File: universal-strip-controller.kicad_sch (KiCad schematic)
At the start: 50 parts, among them J1 Conn_01x03_Pin, J2 Conn_01x02_Pin, SW1 434133025816, SW2 434133025816, U1 RP2350B, U2 RPI RM2, U3 W25Q128JVSIQ, U9 DS3231SN, X1 12MHz

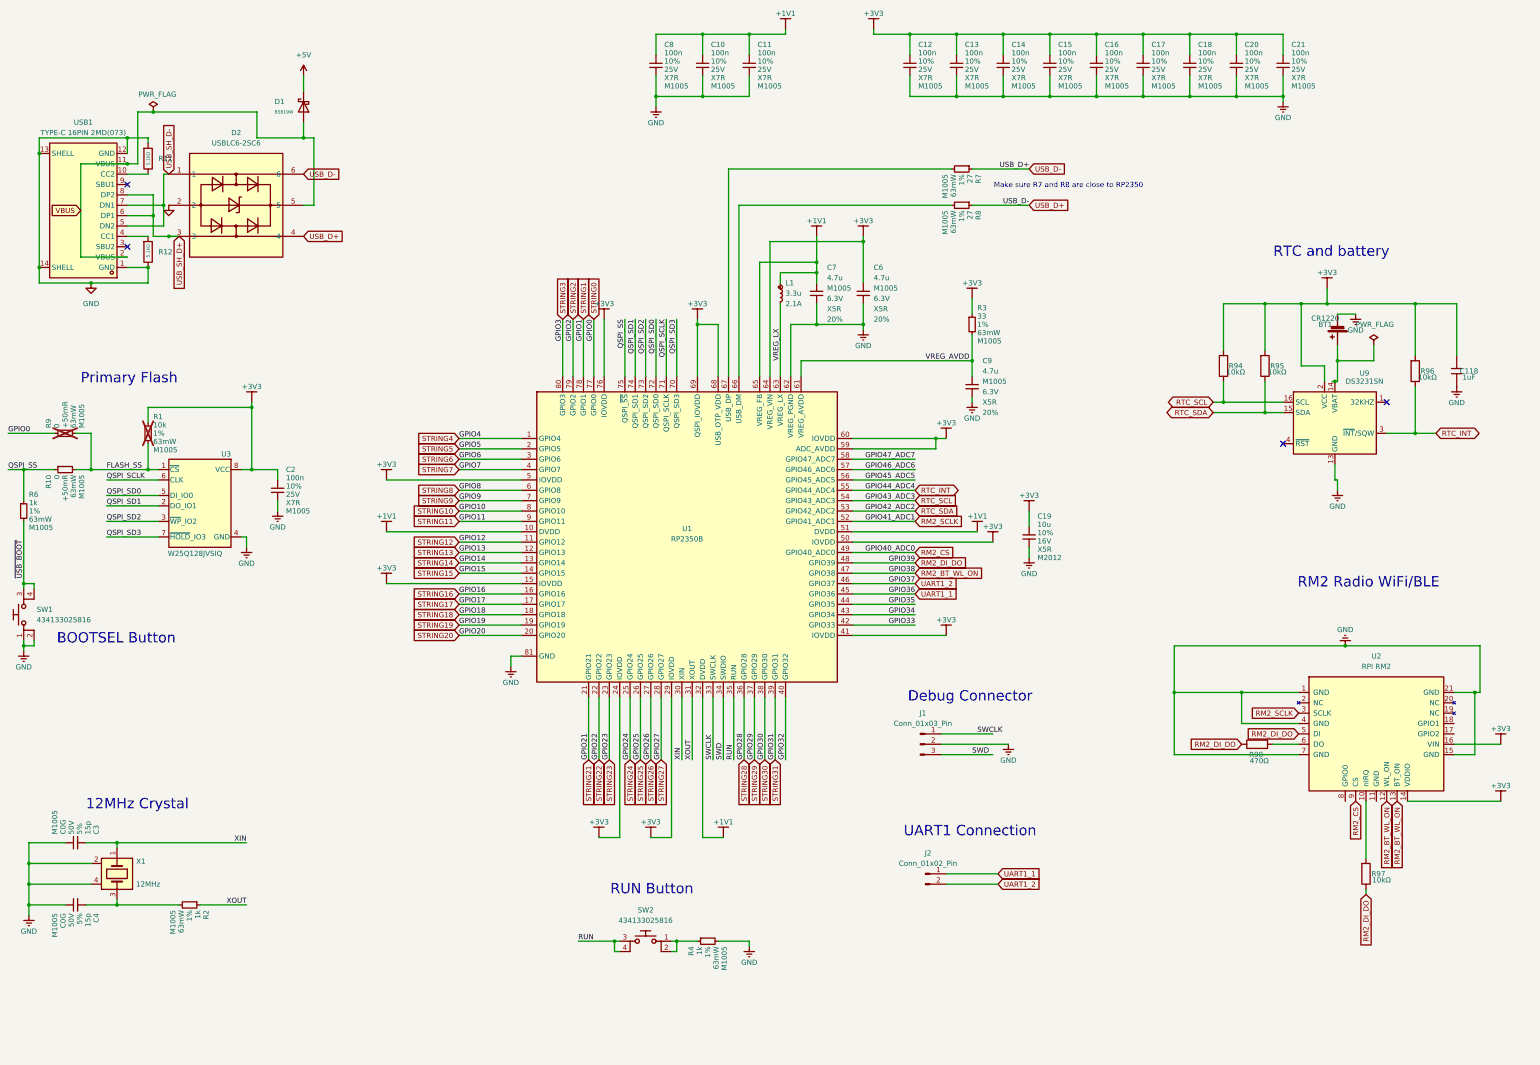
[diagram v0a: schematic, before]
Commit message: Added power, output, and more status LEDs
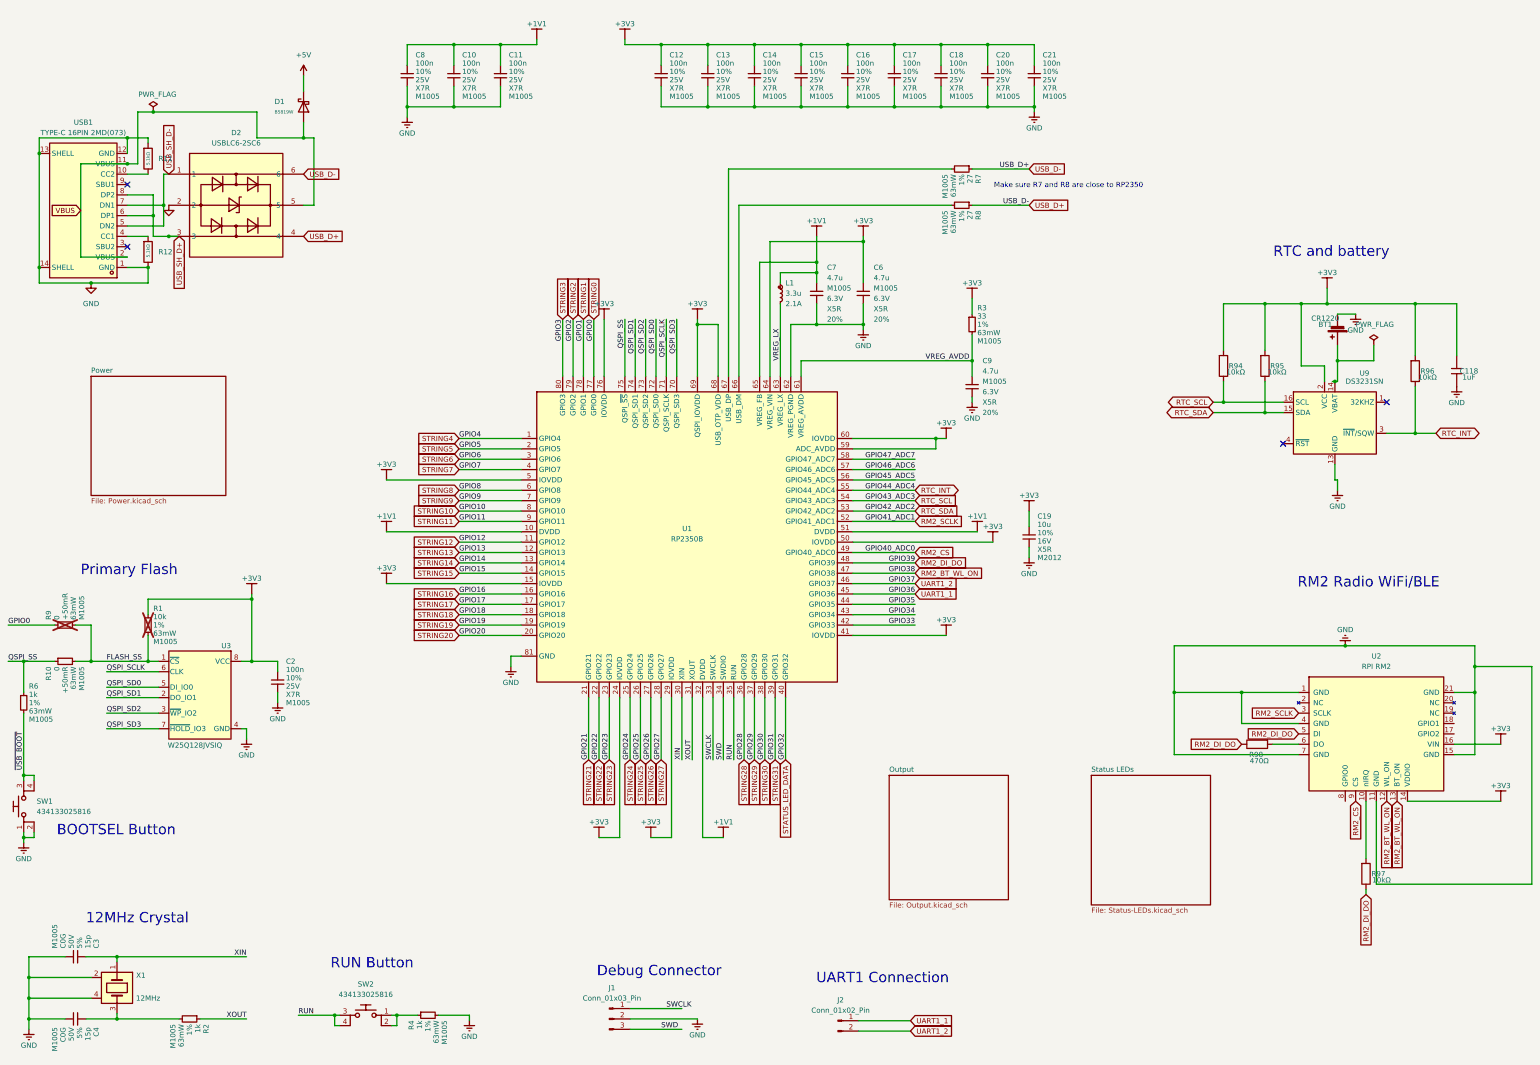
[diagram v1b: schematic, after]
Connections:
- net GND: now also U2.11 (GND)
- net GPIO32 renamed STATUS_LED_DATA
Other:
- added sheet Output (Output.kicad_sch)
- added sheet Power (Power.kicad_sch)
- added sheet Status LEDs (Status-LEDs.kicad_sch)
- moved on the sheet: C10, C11, C12, C13, C14, C15, C16, C17, C18, C2, C20, C21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

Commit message: Fix ERC: register missing libraries, add PWR_FLAGs, rename zone rails
- Register project-local sym-lib-table/fp-lib-table. PixelBlit points at
  pico-pixel's live library; RPI_COMPILED/KiCad_Standard/EasyEDA/PCM_JLCPCB
  footprints vendored (via the abandoned universal-strip-controller-first
  attempt) into libs/; RPI_DB, RPI - Power, EasyEDA, PCM_JLCPCB-Diodes and
  PCM_JLCPCB-Resistors symbols extracted from the schematics' own embedded
  symbol cache into standalone .kicad_sym files, validated with
  `kicad-cli sym upgrade`.
- Fix U1's footprint: RPI_COMPILED:rpi_rp2350b doesn't exist anywhere
  (not even in the original RP2350B-MINIMAL reference) - corrected to
  rpi_rp2350b_vias, the footprint that's actually there.
- Point D10 (BZT52C15V) and R5/R20 (0603s) at KiCad's own standard
  SOD-123/0603 footprints; no vendored copy of their original
  EasyEDA/JLCPCB footprints existed anywhere to source from.
- Add PWR_FLAGs on the 8 nets ERC found undriven: +VIN_Z1-4, +12V_SYS,
  GND (top sheet), +1V1, and VREG_AVDD (U1 pin 61).
- Rename +12V_Z1-4 to +VIN_Z1-4 (zones carry 5-12V depending on what's
  plugged in, not a fixed 12V).

ERC: 1009 violations / 8 errors -> 533 violations / 0 errors.
Remaining warnings are pre-existing: fuse/diode symbols typed
Unspecified instead of Passive (pin_to_pin), intentional dual net
labels (STRINGn/GPIOn etc., except a real USB_D+/USB_D- issue still
open), schematic drawing hygiene (off-grid/dangling wire endpoints),
and symbol-cache drift now visible now that real libraries exist
(lib_symbol_mismatch - fix via Update Symbols from Library in KiCad).
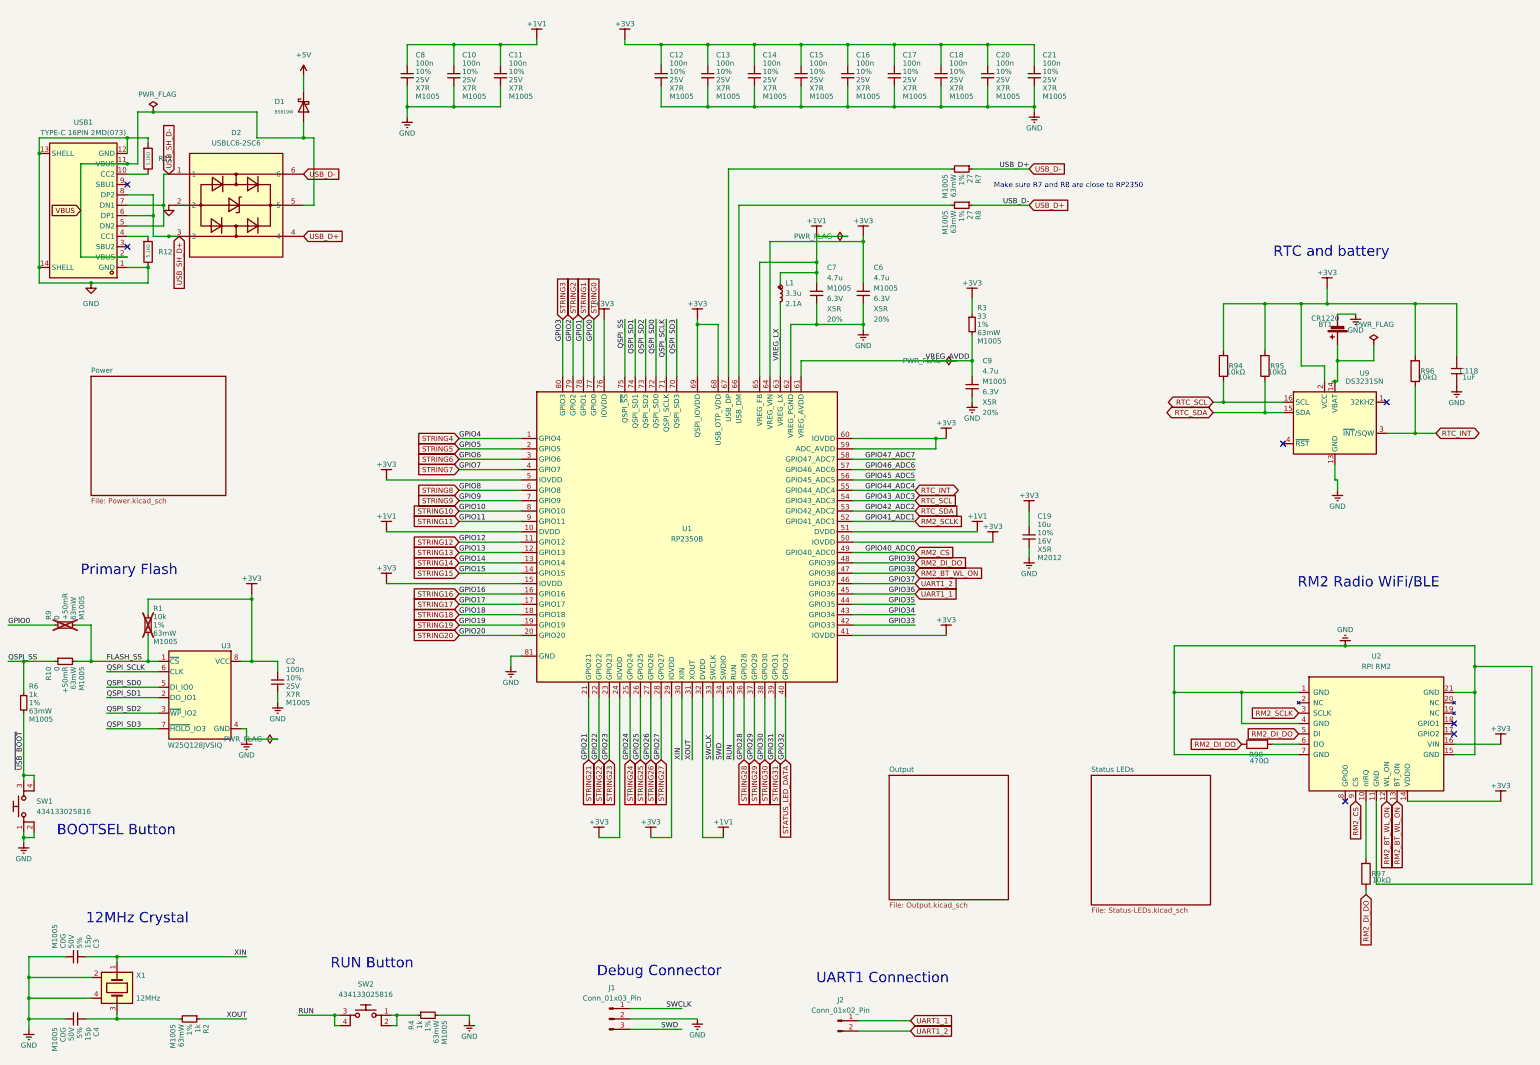
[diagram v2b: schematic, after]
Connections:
- no-connect marks 4 -> 7

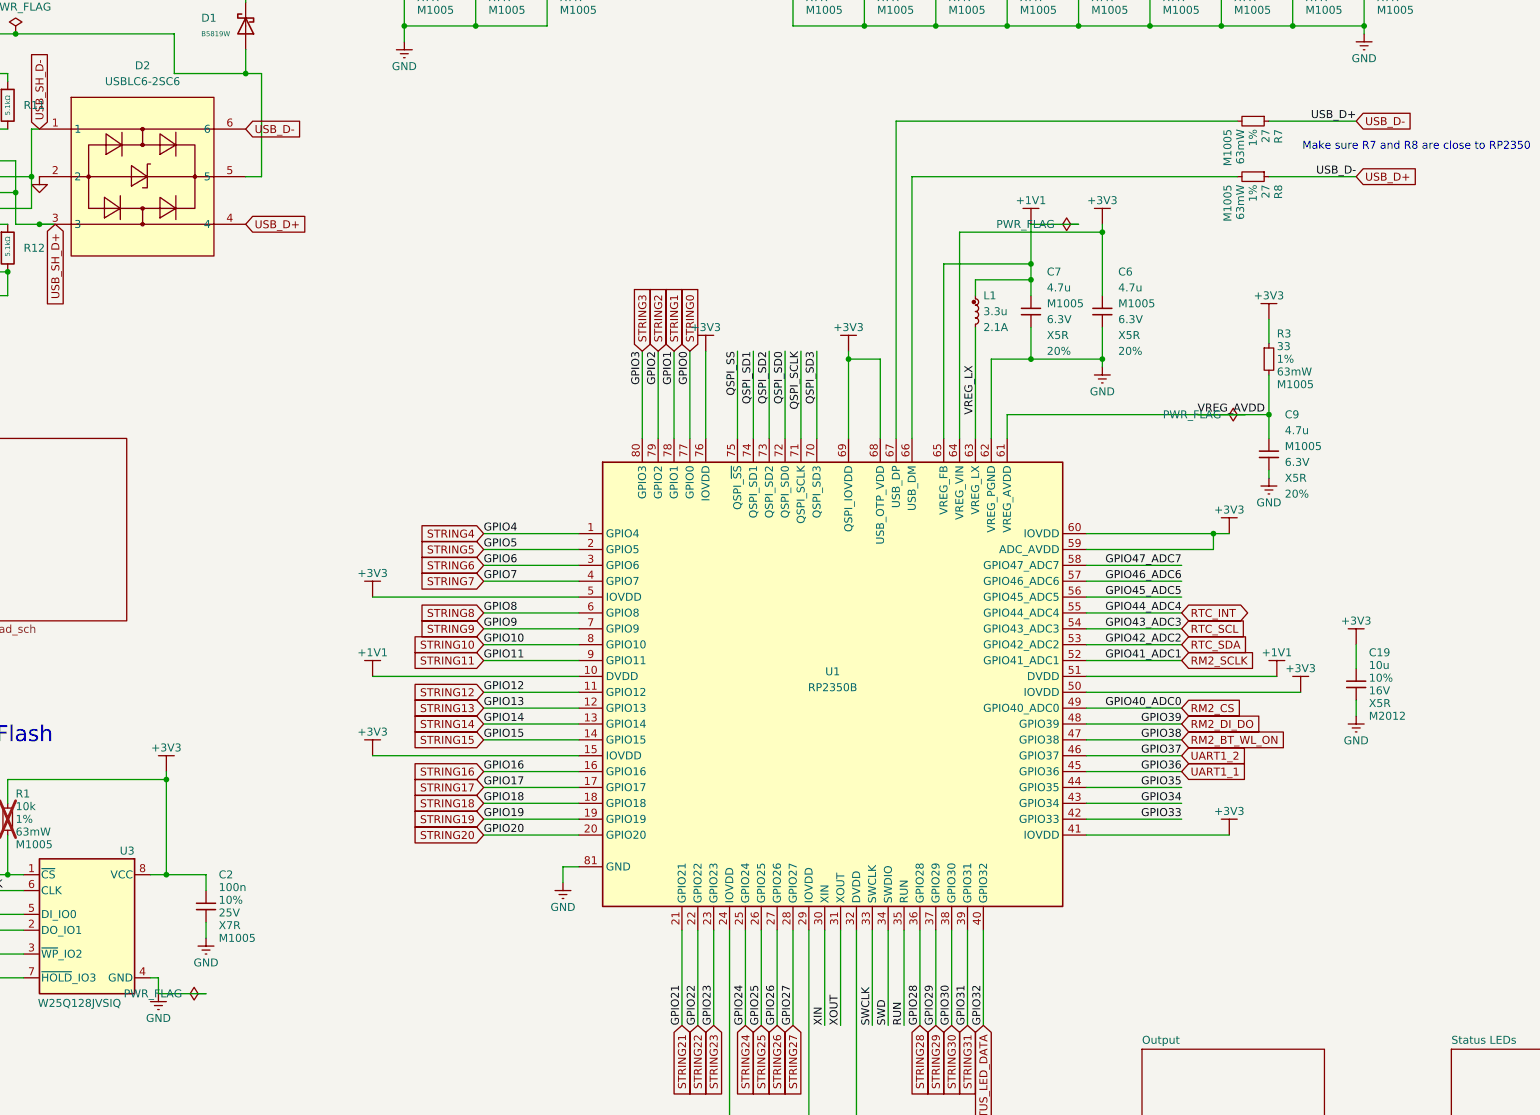
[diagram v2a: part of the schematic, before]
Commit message: Updated symbols from library
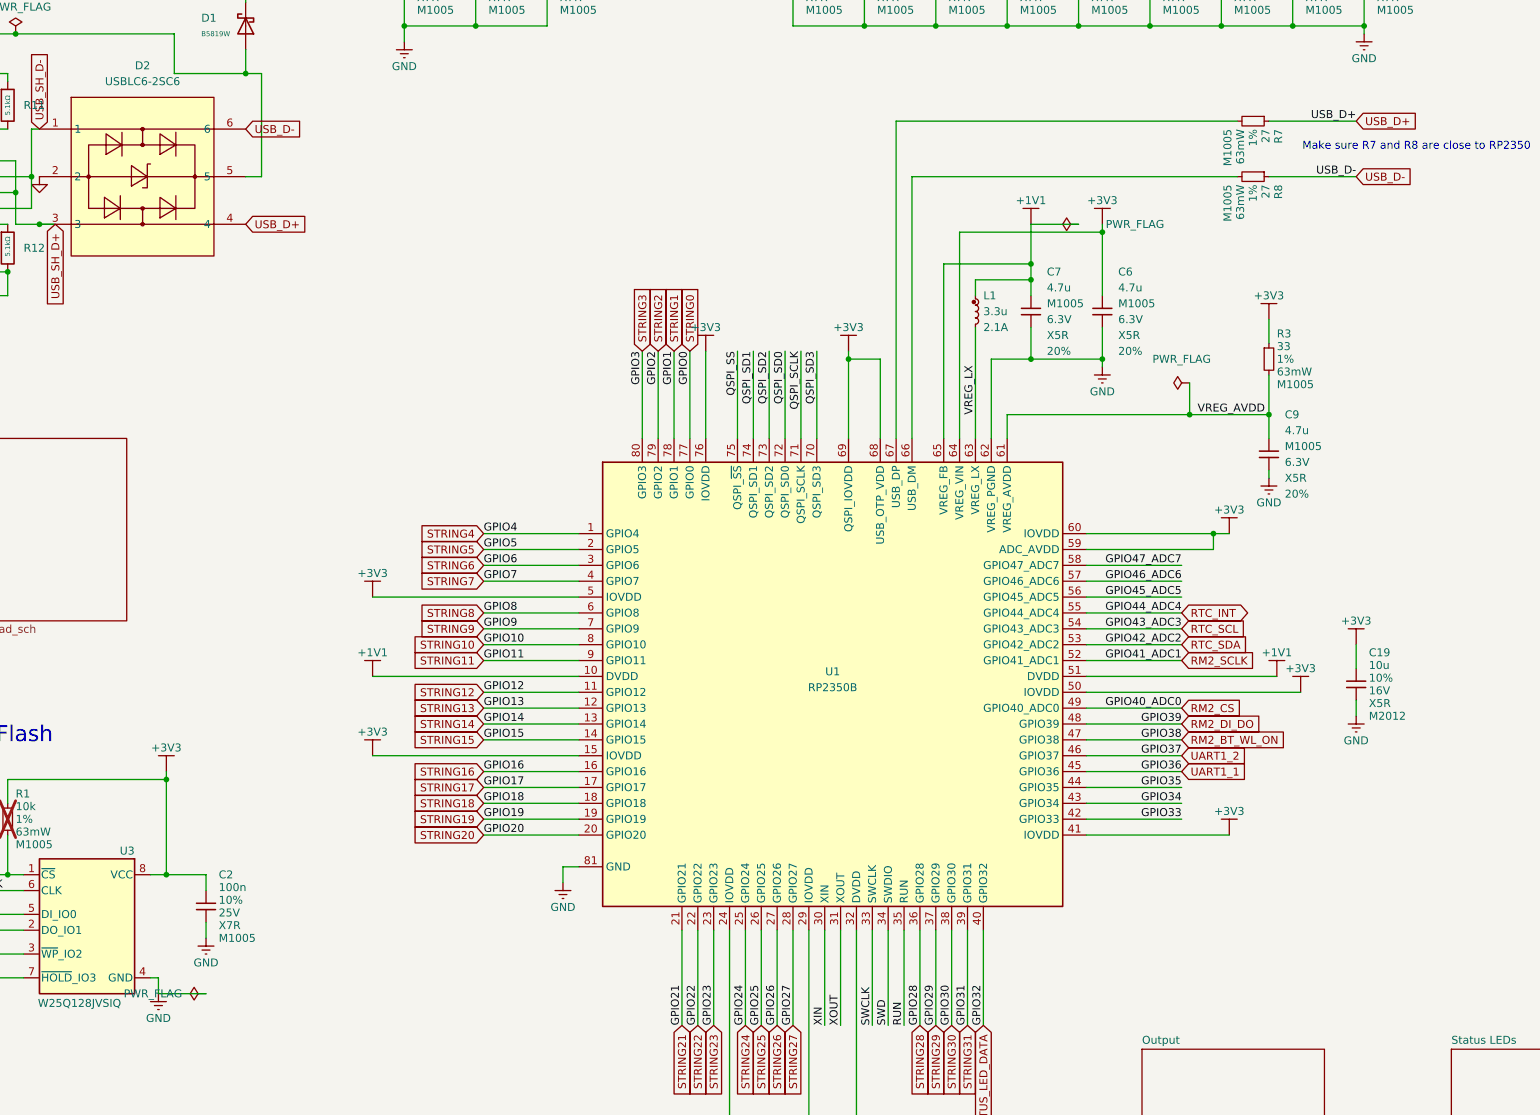
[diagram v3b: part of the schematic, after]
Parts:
- U9: footprint KiCad_Standard:SOIC-16W_7.5x10.3mm_P1.27mm -> Package_SO:SOIC-16W_7.5x10.3mm_P1.27mm
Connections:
- net USB_D+: no longer D2.6, R8.1
- new net USB_D-: D2.6, R8.1
